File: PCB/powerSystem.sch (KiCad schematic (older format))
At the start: 7 parts, among them U201 MCP1703T-5002E/CB, U202 LD2979

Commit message: Trying out an alternative layout
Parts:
- U202: symbol LD2979-RESCUE-TfaC -> LD2979-RESCUE-TfaC-RESCUE-TfaC
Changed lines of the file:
@@
 $EndComp
 $Comp
-L GND #PWR02
+L GND #PWR202
 U 1 1 5565D42B
 P 5000 3050
-F 0 "#PWR02" H 5000 2800 50  0001 C CNN
+F 0 "#PWR202" H 5000 2800 50  0001 C CNN
 F 1 "GND" H 5000 2900 50  0000 C CNN
 F 2 "" H 5000 3050 60  0000 C CNN
@@
 	6350 4500 6350 4800
 $Comp
-L GND #PWR03
+L GND #PWR204
 U 1 1 5565DE90
 P 6350 4800
-F 0 "#PWR03" H 6350 4550 50  0001 C CNN
+F 0 "#PWR204" H 6350 4550 50  0001 C CNN
 F 1 "GND" H 6350 4650 50  0000 C CNN
 F 2 "" H 6350 4800 60  0000 C CNN
@@
 Connection ~ 5000 2950
 $Comp
-L GND #PWR04
+L GND #PWR203
 U 1 1 556C9868
 P 5050 4800
-F 0 "#PWR04" H 5050 4550 50  0001 C CNN
+F 0 "#PWR203" H 5050 4550 50  0001 C CNN
 F 1 "GND" H 5050 4650 50  0000 C CNN
 F 2 "" H 5050 4800 60  0000 C CNN
@@
 $EndComp
 $Comp
-L LD2979-RESCUE-TfaC U202
+L LD2979-RESCUE-TfaC-RESCUE-TfaC U202
 U 1 1 556C9A30
 P 5050 4000
@@
 $EndComp
 $Comp
-L GND #PWR05
+L GND #PWR201
 U 1 1 5565DD5B
 P 3750 4800
-F 0 "#PWR05" H 3750 4550 50  0001 C CNN
+F 0 "#PWR201" H 3750 4550 50  0001 C CNN
 F 1 "GND" H 3750 4650 50  0000 C CNN
 F 2 "" H 3750 4800 60  0000 C CNN

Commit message: small changes
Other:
- note added: "Consider patching this to Vcc rather \nthan Vin due to power dispation \ngoing from say 7V5 Vin to \n3V3 Vbb x 15mA."
- note added: "The power requirement is still not set.\nThe case may have to be changed to allow\nbetter heat disipation."
- moved on the sheet: C202, C203, U201
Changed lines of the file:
@@
 LIBS:valves
 LIBS:Tfac-Symbols
-LIBS:TfaC-cache
 EELAYER 25 0
 EELAYER END
@@
 L MCP1703T-5002E/CB U201
 U 1 1 5565D3BF
-P 5000 2000
-F 0 "U201" H 5100 1850 50  0000 C CNN
-F 1 "MCP1703T-5002E/CB" H 5000 2150 50  0000 C CNN
-F 2 "tfac-footprints:SOT-23A" H 5000 2000 60  0001 C CNN
-F 3 "http://ww1.microchip.com/downloads/en/DeviceDoc/22049e.pdf" H 5000 2000 60  0001 C CNN
-F 4 "MCP1703T-5002E/CB" H 5000 2000 60  0001 C CNN "MPN"
-F 5 "651424 - 62" H 5000 2000 60  0001 C CNN "ConradPN"
-	1    5000 2000
+P 5100 1600
+F 0 "U201" H 5200 1450 50  0000 C CNN
+F 1 "MCP1703T-5002E/CB" H 5100 1750 50  0000 C CNN
+F 2 "tfac-footprints:SOT-23A" H 5100 1600 60  0001 C CNN
+F 3 "http://ww1.microchip.com/downloads/en/DeviceDoc/22049e.pdf" H 5100 1600 60  0001 C CNN
+F 4 "MCP1703T-5002E/CB" H 5100 1600 60  0001 C CNN "MPN"
+F 5 "651424 - 62" H 5100 1600 60  0001 C CNN "ConradPN"
+	1    5100 1600
 	1    0    0    -1
 $EndComp
@@
 L GND #PWR02
 U 1 1 5565D42B
-P 5000 3050
-F 0 "#PWR02" H 5000 2800 50  0001 C CNN
-F 1 "GND" H 5000 2900 50  0000 C CNN
-F 2 "" H 5000 3050 60  0000 C CNN
-F 3 "" H 5000 3050 60  0000 C CNN
-	1    5000 3050
+P 5100 2650
+F 0 "#PWR02" H 5100 2400 50  0001 C CNN
+F 1 "GND" H 5100 2500 50  0000 C CNN
+F 2 "" H 5100 2650 60  0000 C CNN
+F 3 "" H 5100 2650 60  0000 C CNN
+	1    5100 2650
 	1    0    0    -1
 $EndComp
-Text HLabel 3750 2000 0    60   Input ~ 0
+Text HLabel 3850 1600 0    60   Input ~ 0
 Vin
 Wire Wire Line
-	3750 2000 4700 2000
+	3850 1600 4800 1600
 Wire Wire Line
-	5300 2000 6350 2000
+	5400 1600 6450 1600
 Wire Wire Line
 	5500 4000 6600 4000
@@
 	1    0    0    -1
 $EndComp
-Text HLabel 6350 2000 2    60   Output ~ 0
+Text HLabel 6450 1600 2    60   Output ~ 0
 Vcc
 Text HLabel 6600 4000 2    60   Output ~ 0
@@
 Text HLabel 3500 4000 0    60   Input ~ 0
 Vin
-Connection ~ 5000 2950
+Connection ~ 5100 2550
 $Comp
 L GND #PWR04
@@
 L C C202
 U 1 1 556C9E21
-P 4250 2300
-F 0 "C202" H 4275 2400 50  0000 L CNN
-F 1 "1u" H 4275 2200 50  0000 L CNN
-F 2 "Capacitors_SMD:C_0805_HandSoldering" H 4288 2150 30  0001 C CNN
-F 3 "" H 4250 2300 60  0000 C CNN
-F 4 "Value" H 4250 2300 60  0001 C CNN "MPN"
-F 5 "Value" H 4250 2300 60  0001 C CNN "ConradPN"
-	1    4250 2300
+P 4350 1900
+F 0 "C202" H 4375 2000 50  0000 L CNN
+F 1 "1u" H 4375 1800 50  0000 L CNN
+F 2 "Capacitors_SMD:C_0805_HandSoldering" H 4388 1750 30  0001 C CNN
+F 3 "" H 4350 1900 60  0000 C CNN
+F 4 "Value" H 4350 1900 60  0001 C CNN "MPN"
+F 5 "Value" H 4350 1900 60  0001 C CNN "ConradPN"
+	1    4350 1900
 	1    0    0    -1
 $EndComp
@@
 L C C203
 U 1 1 556C9E5C
-P 5650 2300
-F 0 "C203" H 5675 2400 50  0000 L CNN
-F 1 "1u" H 5675 2200 50  0000 L CNN
-F 2 "Capacitors_SMD:C_0805_HandSoldering" H 5688 2150 30  0001 C CNN
-F 3 "" H 5650 2300 60  0000 C CNN
-	1    5650 2300
+P 5750 1900
+F 0 "C203" H 5775 2000 50  0000 L CNN
+F 1 "1u" H 5775 1800 50  0000 L CNN
+F 2 "Capacitors_SMD:C_0805_HandSoldering" H 5788 1750 30  0001 C CNN
+F 3 "" H 5750 1900 60  0000 C CNN
+	1    5750 1900
 	1    0    0    -1
 $EndComp
 Wire Wire Line
-	5000 2200 5000 3050
+	5100 1800 5100 2650
 Wire Wire Line
-	4250 2450 4250 2950
+	4350 2050 4350 2550
 Wire Wire Line
-	5650 2950 5650 2450
+	5750 2550 5750 2050
 Connection ~ 3750 4000
 Wire Wire Line
@@
 	3750 4500 3750 4800
 Wire Wire Line
-	4250 2150 4250 2000
-Connection ~ 4250 2000
+	4350 1750 4350 1600
+Connection ~ 4350 1600
 Wire Wire Line
-	5650 2150 5650 2000
-Connection ~ 5650 2000
+	5750 1750 5750 1600
+Connection ~ 5750 1600
 Wire Wire Line
 	6350 4200 6350 4000
 Connection ~ 6350 4000
 Wire Wire Line
-	4250 2950 5650 2950
+	4350 2550 5750 2550
+Text Notes 3400 3850 0    60   ~ 0
+Consider patching this to Vcc rather \nthan Vin due to power dispation \ngoing from say 7V5 Vin to \n3V3 Vbb x 15mA.
+Text Notes 4300 1300 0    60   ~ 0
+The power requirement is still not set.\nThe case may have to be changed to allow\nbetter heat disipation.
 $EndSCHEMATC

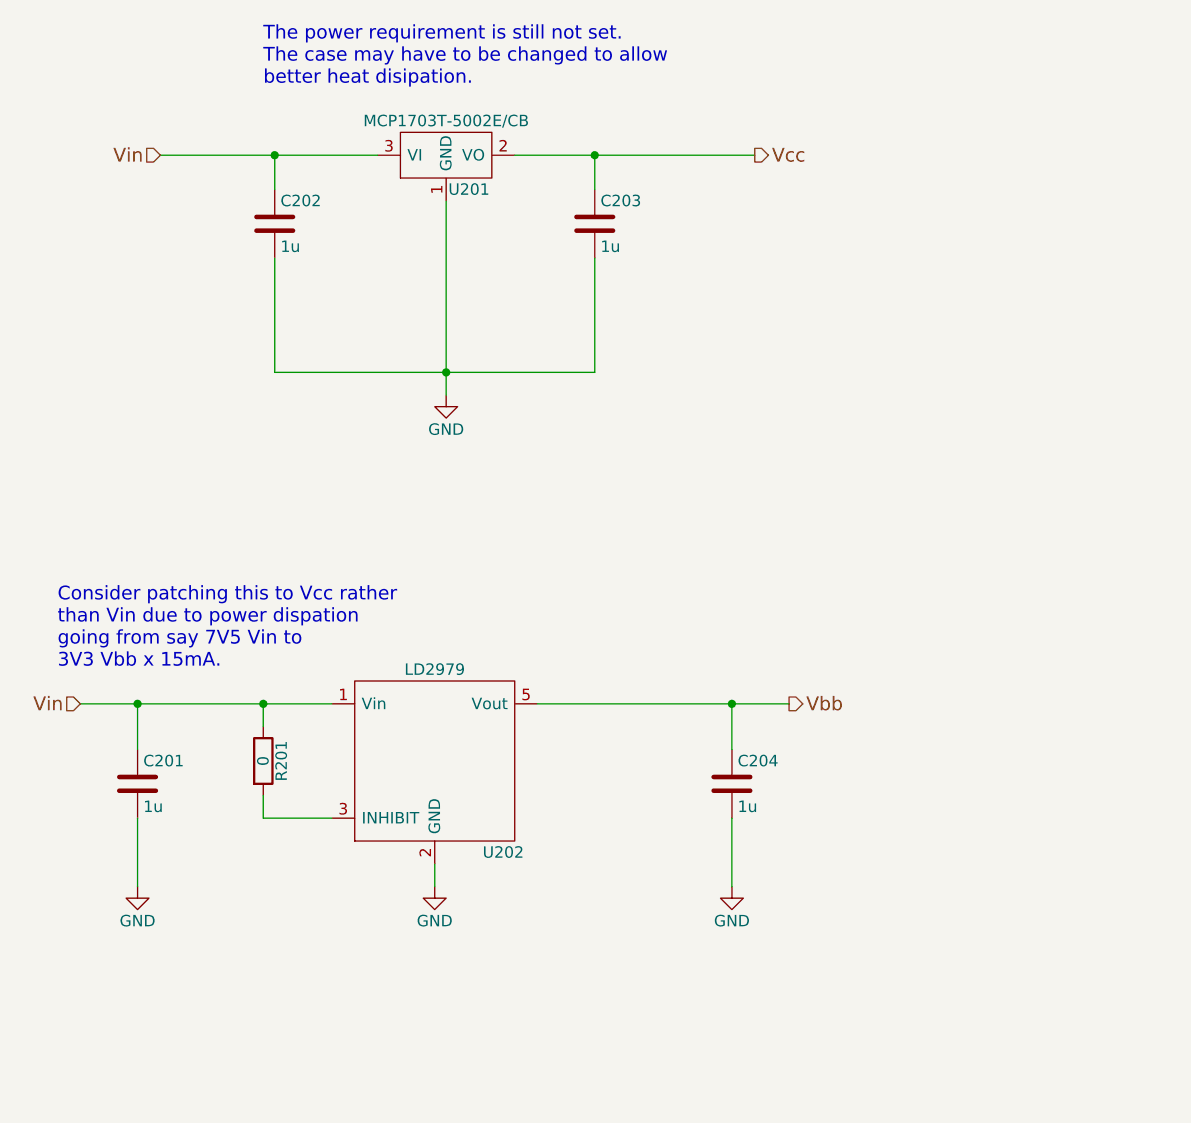
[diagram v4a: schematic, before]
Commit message: Added indicator LEDs and Heartbeat
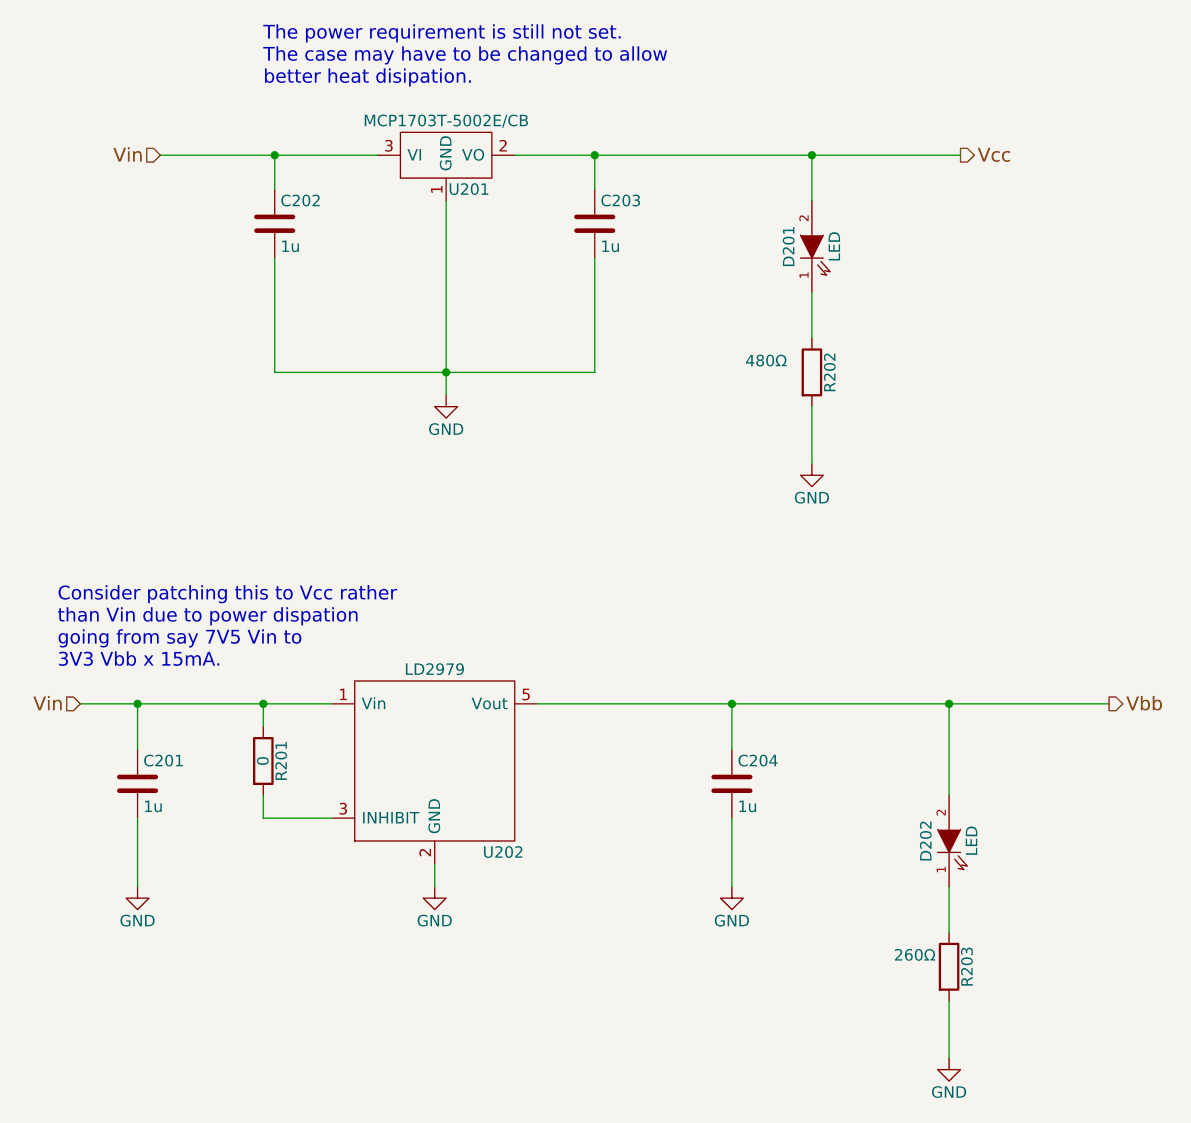
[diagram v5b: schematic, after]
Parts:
- added D201, D202: LED, LEDs:LED-0805, symbol LED
- added R202: 480Ω, Resistors_SMD:R_0805_HandSoldering, symbol R
- added R203: 260Ω, Resistors_SMD:R_0805_HandSoldering, symbol R
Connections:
- net GND: now also R202.2, R203.2
- net Vbb: now also D202.2 (A)
- net Vcc: now also D201.2 (A)
- new net: D201.1 (K), R202.1
- new net: D202.1 (K), R203.1
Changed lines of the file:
@@
 LIBS:valves
 LIBS:Tfac-Symbols
+LIBS:TfaC-cache
 EELAYER 25 0
 EELAYER END
@@
 	3850 1600 4800 1600
 Wire Wire Line
-	5400 1600 6450 1600
-Wire Wire Line
-	5500 4000 6600 4000
+	5400 1600 7350 1600
+Wire Wire Line
+	5500 4000 8000 4000
 $Comp
 L C C204
@@
 	1    0    0    -1
 $EndComp
-Text HLabel 6450 1600 2    60   Output ~ 0
+Text HLabel 7350 1600 2    60   Output ~ 0
 Vcc
-Text HLabel 6600 4000 2    60   Output ~ 0
+Text HLabel 8000 4000 2    60   Output ~ 0
 Vbb
 Text HLabel 3500 4000 0    60   Input ~ 0
@@
 Text Notes 4300 1300 0    60   ~ 0
 The power requirement is still not set.\nThe case may have to be changed to allow\nbetter heat disipation.
+$Comp
+L LED D201
+U 1 1 564D71D7
+P 6700 2000
+F 0 "D201" H 6700 2100 50  0000 C CNN
+F 1 "LED" H 6700 1900 50  0000 C CNN
+F 2 "LEDs:LED-0805" H 6700 2000 60  0001 C CNN
+F 3 "" H 6700 2000 60  0000 C CNN
+	1    6700 2000
+	0    -1   -1   0
+$EndComp
+$Comp
+L R R202
+U 1 1 564D7317
+P 6700 2550
+F 0 "R202" V 6780 2550 50  0000 C CNN
+F 1 "480Ω" H 6500 2600 50  0000 C CNN
+F 2 "Resistors_SMD:R_0805_HandSoldering" V 6630 2550 30  0001 C CNN
+F 3 "" H 6700 2550 30  0000 C CNN
+	1    6700 2550
+	1    0    0    -1
+$EndComp
+Wire Wire Line
+	6700 1600 6700 1800
+Connection ~ 6700 1600
+Wire Wire Line
+	6700 2200 6700 2400
+$Comp
+L GND #PWR06
+U 1 1 564D7417
+P 6700 2950
+F 0 "#PWR06" H 6700 2700 50  0001 C CNN
+F 1 "GND" H 6700 2800 50  0000 C CNN
+F 2 "" H 6700 2950 60  0000 C CNN
+F 3 "" H 6700 2950 60  0000 C CNN
+	1    6700 2950
+	1    0    0    -1
+$EndComp
+Wire Wire Line
+	6700 2700 6700 2950
+$Comp
+L LED D202
+U 1 1 564D751D
+P 7300 4600
+F 0 "D202" H 7300 4700 50  0000 C CNN
+F 1 "LED" H 7300 4500 50  0000 C CNN
+F 2 "LEDs:LED-0805" H 7300 4600 60  0001 C CNN
+F 3 "" H 7300 4600 60  0000 C CNN
+	1    7300 4600
+	0    -1   -1   0
+$EndComp
+$Comp
+L R R203
+U 1 1 564D7523
+P 7300 5150
+F 0 "R203" V 7380 5150 50  0000 C CNN
+F 1 "260Ω" H 7150 5200 50  0000 C CNN
+F 2 "Resistors_SMD:R_0805_HandSoldering" V 7230 5150 30  0001 C CNN
+F 3 "" H 7300 5150 30  0000 C CNN
+	1    7300 5150
+	1    0    0    -1
+$EndComp
+Wire Wire Line
+	7300 4000 7300 4400
+Wire Wire Line
+	7300 4800 7300 5000
+$Comp
+L GND #PWR07
+U 1 1 564D752B
+P 7300 5550
+F 0 "#PWR07" H 7300 5300 50  0001 C CNN
+F 1 "GND" H 7300 5400 50  0000 C CNN
+F 2 "" H 7300 5550 60  0000 C CNN
+F 3 "" H 7300 5550 60  0000 C CNN
+	1    7300 5550
+	1    0    0    -1
+$EndComp
+Wire Wire Line
+	7300 5300 7300 5550
+Connection ~ 7300 4000
 $EndSCHEMATC
